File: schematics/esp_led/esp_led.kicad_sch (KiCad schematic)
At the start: 31 parts, among them J1 ESP32-WROOM-DevKit, J3 BOOMELE PH-4A, J4 DC-005C-20A, J5 BOOMELE PH-4A, Q1 FDV303N, Q2 FDV303N, Q3 FDV303N, Q4 FDV303N, Q5 FDV303N, Q6 FDV303N, SW1 SW_DPST, SW2 Color_Button, SW3 Color_Selector, U1 LM2596S-5

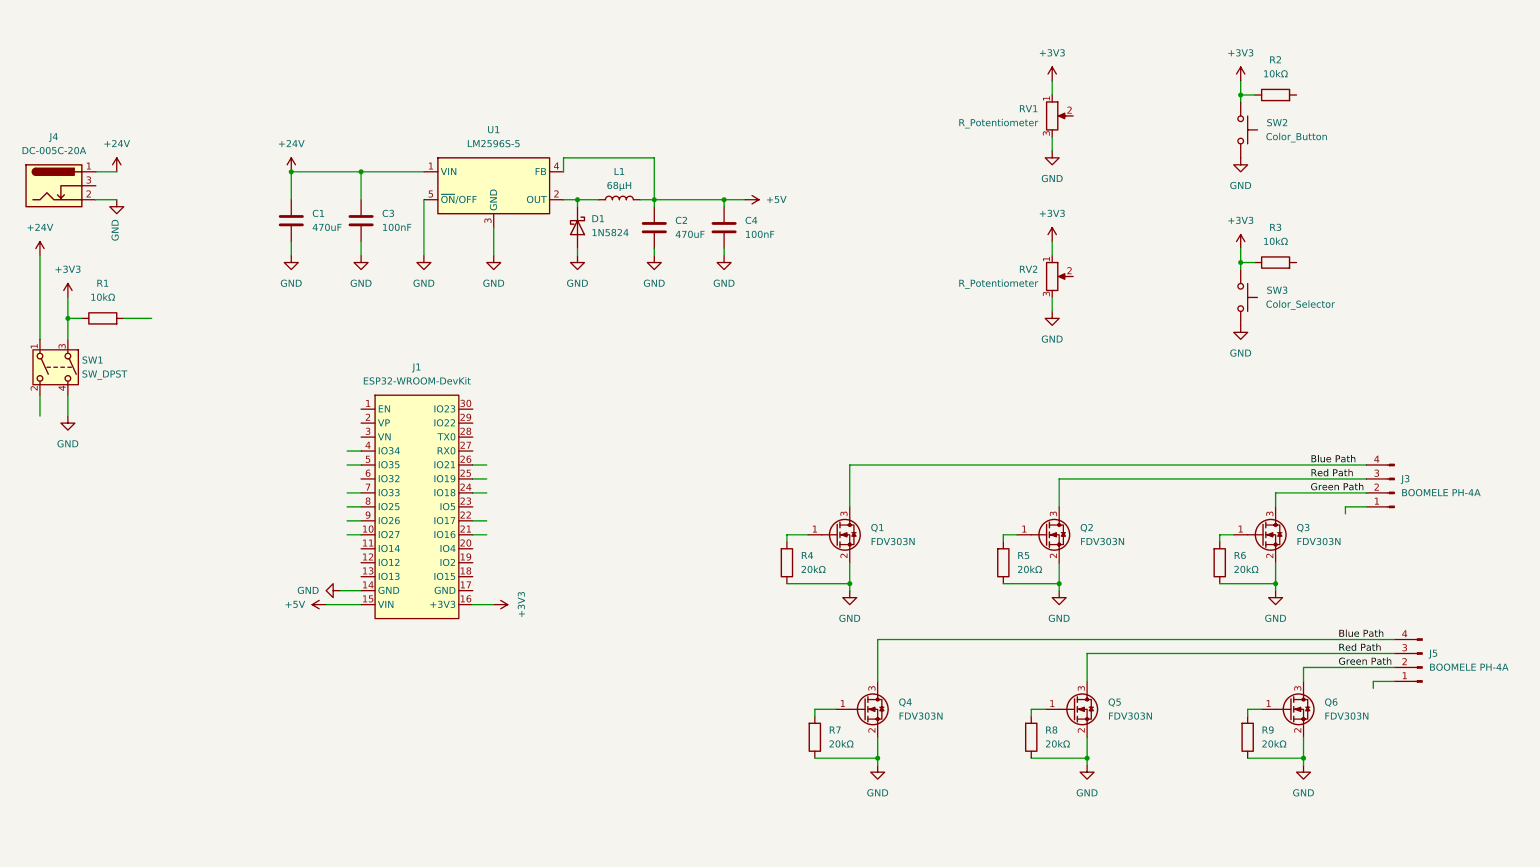
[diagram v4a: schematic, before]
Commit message: The first draft of the PCB. I tried my best to do it kind of clean with 4 copper layers. I also moved the channel outputs for LED 1 a little to make pathing easier.
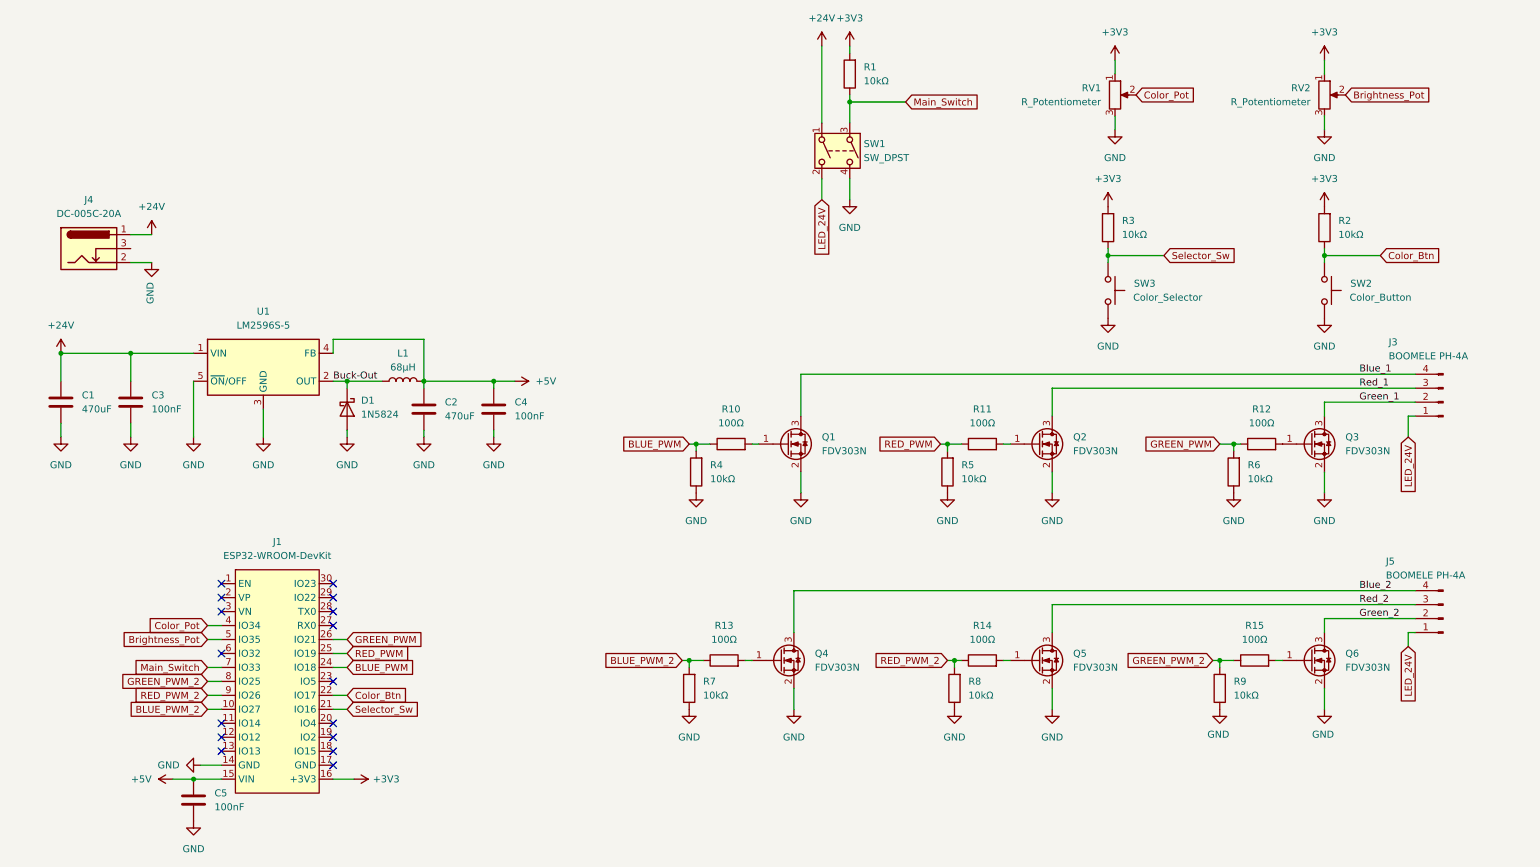
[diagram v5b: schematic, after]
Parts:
- removed R4, R5, R6, R7, R8, R9: 20kΩ, Resistor_SMD:R_0201_0603Metric, symbol Resistor:0603WAF2002T5E
- added C5: 100nF, Capacitor_SMD:C_0201_0603Metric, symbol Device:C
- added R10, R11, R12, R13, R14, R15: 100Ω, Resistor_SMD:R_0201_0603Metric, symbol Device:R
- added R4, R5, R6, R7, R8, R9: 10kΩ, Resistor_SMD:R_0201_0603Metric, symbol Device:R
- J1: footprint Connector_PinSocket_2.00mm:PinSocket_1x15_P2.00mm_Vertical -> Custom:ESP32-32-Devkit-30-Pin
- R1, R2, R3: footprint (none) -> Resistor_SMD:R_0201_0603Metric; MFR.Part # (none) -> 0603WAF1002T5E; Manufacturer (none) -> UNI-ROYAL(Uniroyal Elec)
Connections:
- net +3V3: now also R1.2, R2.2, R3.2; no longer R1.1, R2.1, R3.1, SW1.3, SW2.1, SW3.1
- net +5V: now also C5.1
- net GND: now also C5.2, R4.1, R5.1, R6.1, R7.1, R8.1, R9.1
- net at Q3.1 (G): now also R12.2
- net at Q2.1 (G): now also R11.2
- net LED_24V: now reaches J5.1 (Pin_1)
- net LED_24V: now also J3.1 (Pin_1), SW1.2
- net at Q4.1 (G): now also R13.2
- net at Q5.1 (G): now also R14.2
- net Buck-Out: now reaches D1.1 (K), L1.1, U1.2 (OUT)
- net at Q1.1 (G): now also R10.2
- net Color_Pot: now reaches RV1.2
- net Color_Pot: now also J1.4 (IO34)
- net at Q6.1 (G): now also R15.2
- net BLUE_PWM_2: now reaches J1.10 (IO27)
- net BLUE_PWM_2: now also R13.1, R7.2
- net Selector_Sw: now reaches J1.21 (IO16)
- net Selector_Sw: now also R3.1, SW3.1
- net Color_Btn: now reaches J1.22 (IO17)
- net Color_Btn: now also R2.1, SW2.1
- net BLUE_PWM: now reaches J1.24 (IO18)
- net BLUE_PWM: now also R10.1, R4.2
- net RED_PWM: now reaches J1.25 (IO19)
- net RED_PWM: now also R11.1, R5.2
- net GREEN_PWM: now reaches J1.26 (IO21)
- net GREEN_PWM: now also R12.1, R6.2
- net Brightness_Pot: now reaches J1.5 (IO35)
- net Brightness_Pot: now also RV2.2
- net Main_Switch: now reaches J1.7 (IO33)
- net Main_Switch: now also R1.1, SW1.3
- net GREEN_PWM_2: now reaches J1.8 (IO25)
- net GREEN_PWM_2: now also R15.1, R9.2
- net RED_PWM_2: now reaches J1.9 (IO26)
- net RED_PWM_2: now also R14.1, R8.2
- net Blue Path renamed Blue_1
- net Blue_1: no longer J5.4 (Pin_4), Q4.3 (D)
- net Green Path renamed Green_1
- net Green_1: no longer J5.2 (Pin_2), Q6.3 (D)
- net Red Path renamed Red_1
- net Red_1: no longer J5.3 (Pin_3), Q5.3 (D)
- new net Blue_2: J5.4 (Pin_4), Q4.3 (D)
- new net Green_2: J5.2 (Pin_2), Q6.3 (D)
- new net Red_2: J5.3 (Pin_3), Q5.3 (D)
- no-connect marks 0 -> 16
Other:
- moved on the sheet: C1, C2, C3, C4, D1, J1, J3, J4, J5, L1, Q1, Q2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
